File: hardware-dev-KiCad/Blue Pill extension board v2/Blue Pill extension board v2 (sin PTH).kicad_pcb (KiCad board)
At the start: 2 copper layers, 68 x 85 mm, 14 parts, among them J1 NRF_MODULE, J2 Conn_02x20_Odd_Even, J3 SD_CARD, J4 Conn_02x20_Odd_Even, J5 GPS_MODULE, J6 HUM & TEMP SENSOR, U1 YAAJ_BluePill_Part_Like

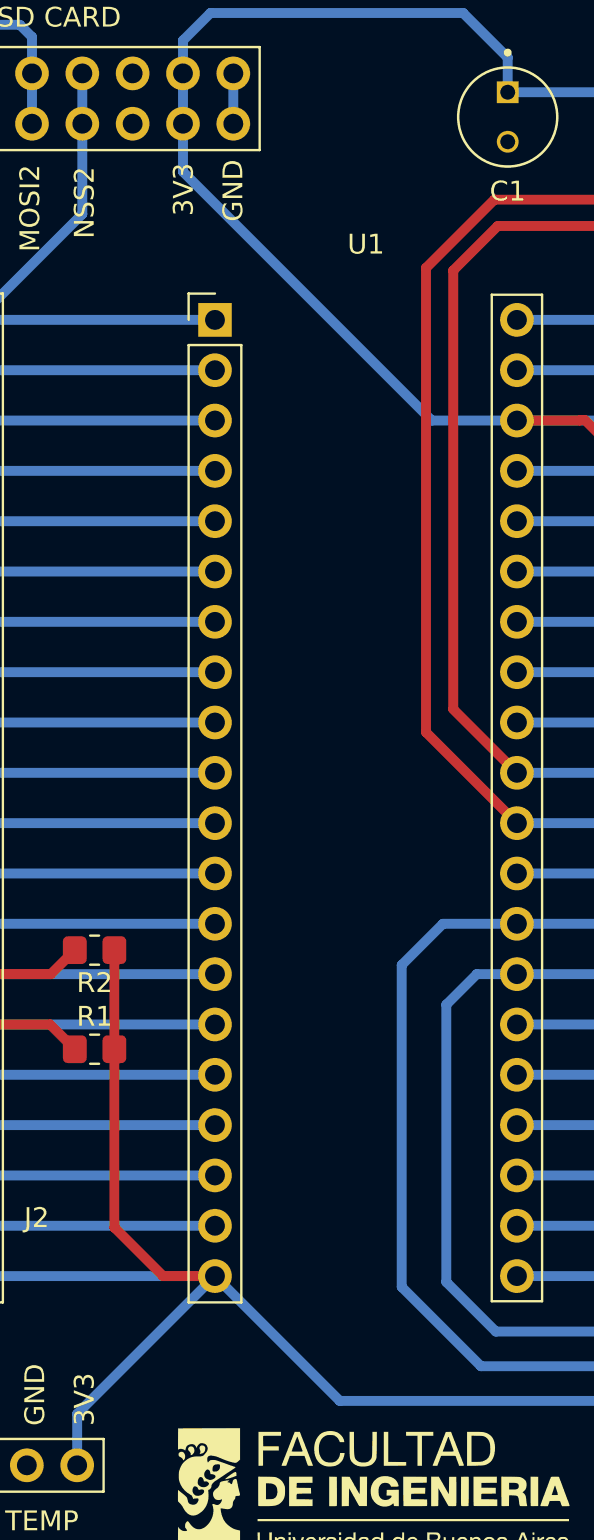
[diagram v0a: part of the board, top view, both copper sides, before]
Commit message: Cambios de routeo y añado PCB para funcionar sin PTH
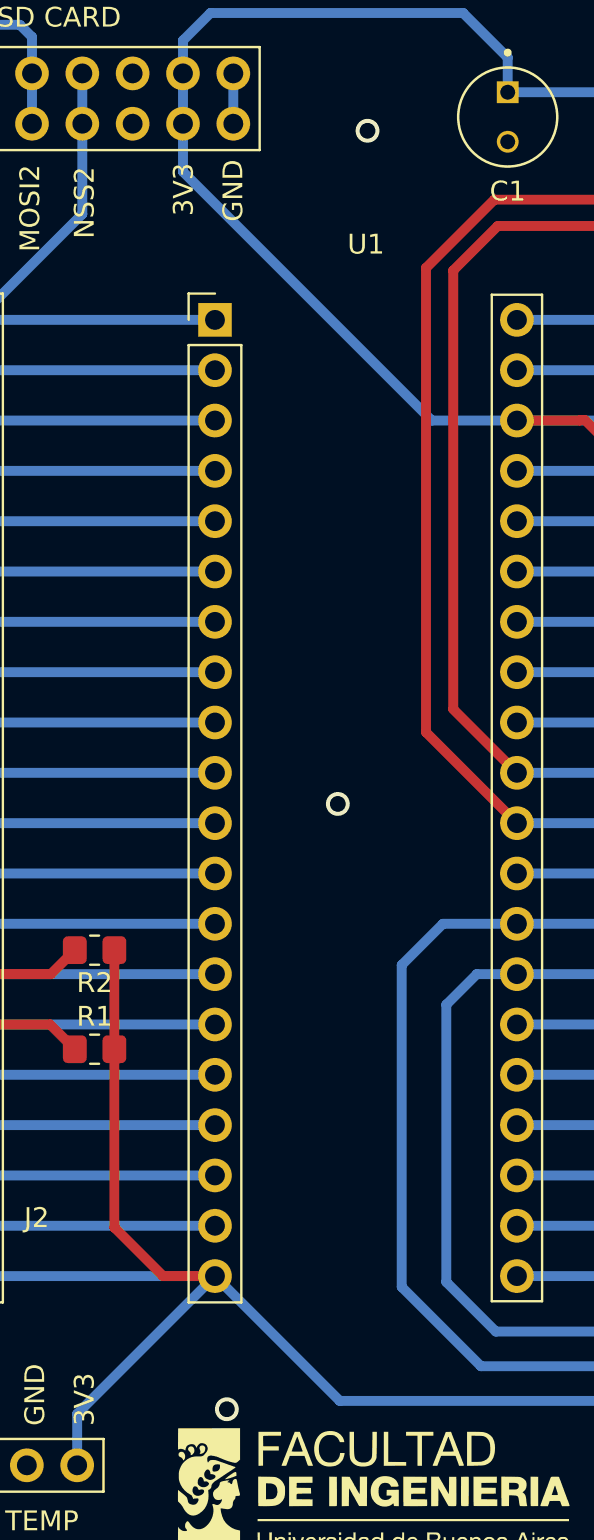
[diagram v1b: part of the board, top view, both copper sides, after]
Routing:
- net GND: vias 0 -> 3
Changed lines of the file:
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@@
 			(outputformat 1)
 			(mirror no)
-			(drillshape 1)
+			(drillshape 0)
 			(scaleselection 1)
-			(outputdirectory "")
+			(outputdirectory "Output-LCI/")
 		)
 	)
@@
 		(net 30)
 	)
+	(via
+		(at 145.45 90.9)
+		(size 1.2)
+		(drill 0.8)
+		(layers "F.Cu" "B.Cu")
+		(free yes)
+		(net 31)
+	)
+	(via
+		(at 146.95 56.925)
+		(size 1.2)
+		(drill 0.8)
+		(layers "F.Cu" "B.Cu")
+		(free yes)
+		(net 31)
+	)
+	(via
+		(at 139.85 121.45)
+		(size 1.2)
+		(drill 0.8)
+		(layers "F.Cu" "B.Cu")
+		(free yes)
+		(net 31)
+	)
 	(segment
